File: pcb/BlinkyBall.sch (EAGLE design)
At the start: 18 parts, among them U1 Tiny85-20-SMT

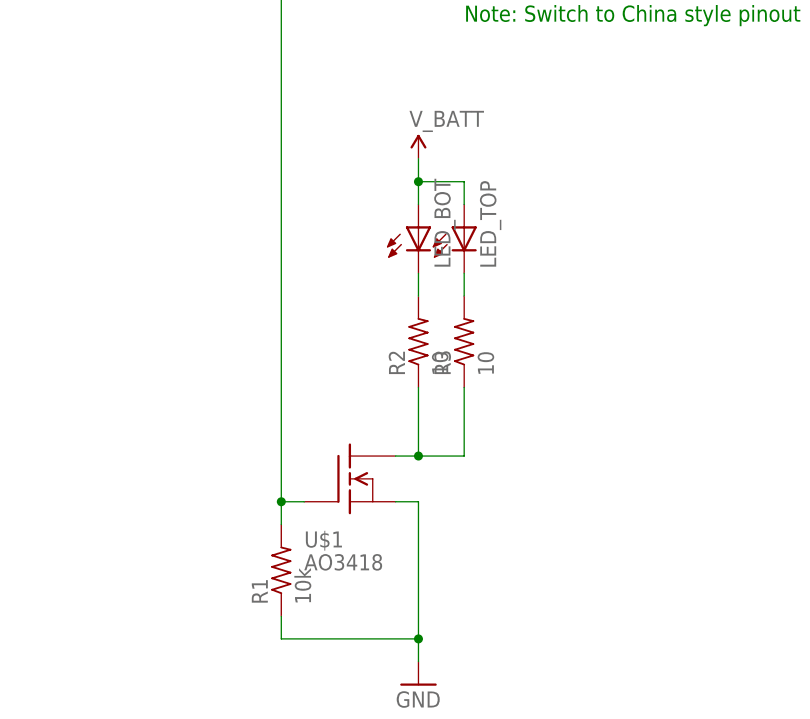
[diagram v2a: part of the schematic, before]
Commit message: PCB: Fix referene names
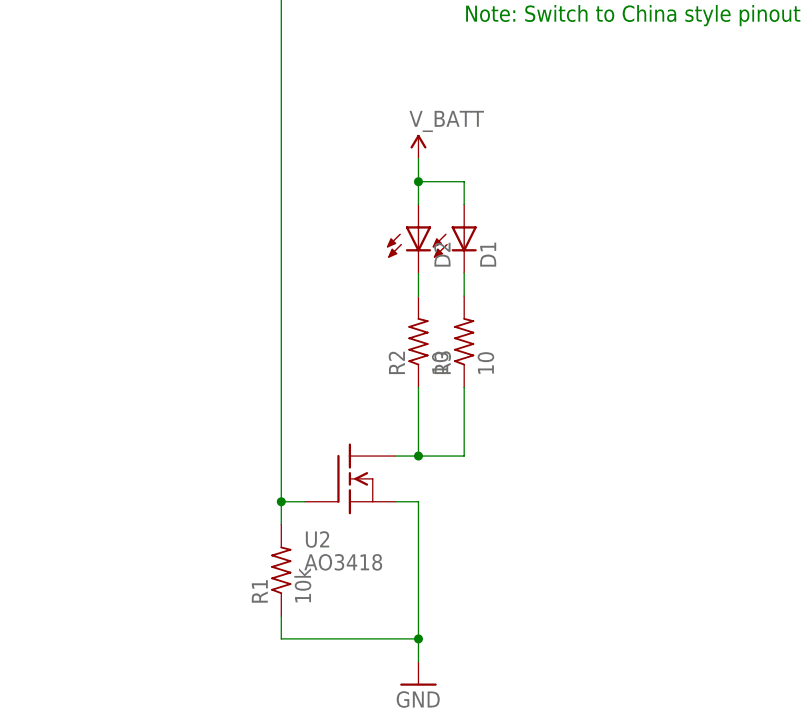
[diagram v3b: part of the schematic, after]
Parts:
- renumbered LED_BOT to D2, LED_TOP to D1, U$1 to U2, U$2 to J2, U$3 to J1, U$5 to U3
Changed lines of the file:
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@@
 <parts>
 <part name="U1" library="SparkFun-DigitalIC" deviceset="ATTINY45" device="TINY85-20-SMT" value="Tiny85-20-SMT"/>
-<part name="U$2" library="blinkinlabs" deviceset="BATTERY_BUTTON_CELL" device="AG3" value="BATTERY_BUTTON_CELLAG3"/>
+<part name="J2" library="blinkinlabs" deviceset="BATTERY_BUTTON_CELL" device="AG3" value="BATTERY_BUTTON_CELLAG3"/>
 <part name="SUPPLY1" library="SparkFun-Aesthetics" deviceset="V_BATT" device=""/>
 <part name="GND1" library="SparkFun-Aesthetics" deviceset="GND" device=""/>
@@
 <part name="GND2" library="SparkFun-Aesthetics" deviceset="GND" device=""/>
 <part name="C1" library="adafruit" deviceset="C-US" device="C0603" value="100nF"/>
-<part name="U$5" library="blinkinlabs" deviceset="TSOP321" device=""/>
+<part name="U3" library="blinkinlabs" deviceset="TSOP321" device=""/>
 <part name="R2" library="adafruit" deviceset="R-US_" device="R0603" value="10"/>
 <part name="R3" library="adafruit" deviceset="R-US_" device="R0603" value="10"/>
@@
 <part name="TP5" library="SparkFun-Passives" deviceset="TEST-POINT" device="3X5"/>
 <part name="TP6" library="SparkFun-Passives" deviceset="TEST-POINT" device="3X5"/>
-<part name="LED_BOT" library="adafruit" deviceset="LED" device="5MM"/>
-<part name="LED_TOP" library="adafruit" deviceset="LED" device="5MM"/>
+<part name="D2" library="adafruit" deviceset="LED" device="5MM"/>
+<part name="D1" library="adafruit" deviceset="LED" device="5MM"/>
 <part name="GND5" library="SparkFun-Aesthetics" deviceset="GND" device=""/>
-<part name="U$1" library="blinkinlabs" deviceset="N_MOSFET" device="SOT23" value="AO3418"/>
+<part name="U2" library="blinkinlabs" deviceset="N_MOSFET" device="SOT23" value="AO3418"/>
 <part name="SUPPLY5" library="SparkFun-Aesthetics" deviceset="V_BATT" device=""/>
 <part name="R1" library="adafruit" deviceset="R-US_" device="R0603" value="10k"/>
 <part name="GND4" library="SparkFun-Aesthetics" deviceset="GND" device=""/>
-<part name="U$3" library="blinkinlabs" deviceset="SW-18015P" device=""/>
+<part name="J1" library="blinkinlabs" deviceset="SW-18015P" device=""/>
 </parts>
 <sheets>
@@
 <instances>
 <instance part="U1" gate="G$1" x="30.48" y="68.58"/>
-<instance part="U$2" gate="G$1" x="-33.02" y="68.58"/>
+<instance part="J2" gate="G$1" x="-33.02" y="68.58"/>
 <instance part="SUPPLY1" gate="G$1" x="-33.02" y="83.82"/>
 <instance part="GND1" gate="1" x="-33.02" y="53.34"/>
@@
 <instance part="GND2" gate="1" x="7.62" y="50.8"/>
 <instance part="C1" gate="G$1" x="12.7" y="71.12"/>
-<instance part="U$5" gate="G$1" x="116.84" y="68.58"/>
+<instance part="U3" gate="G$1" x="116.84" y="68.58"/>
 <instance part="R2" gate="G$1" x="93.98" y="25.4" rot="R90"/>
 <instance part="R3" gate="G$1" x="99.06" y="25.4" rot="R90"/>
@@
 <instance part="TP5" gate="G$1" x="2.54" y="63.5" rot="R180"/>
 <instance part="TP6" gate="G$1" x="45.72" y="83.82" rot="R90"/>
-<instance part="LED_BOT" gate="G$1" x="93.98" y="38.1"/>
-<instance part="LED_TOP" gate="G$1" x="99.06" y="38.1"/>
+<instance part="D2" gate="G$1" x="93.98" y="38.1"/>
+<instance part="D1" gate="G$1" x="99.06" y="38.1"/>
 <instance part="GND5" gate="1" x="93.98" y="-12.7"/>
-<instance part="U$1" gate="G$1" x="83.82" y="10.16"/>
+<instance part="U2" gate="G$1" x="83.82" y="10.16"/>
 <instance part="SUPPLY5" gate="G$1" x="93.98" y="45.72"/>
 <instance part="R1" gate="G$1" x="78.74" y="0" rot="R90"/>
 <instance part="GND4" gate="1" x="99.06" y="73.66"/>
-<instance part="U$3" gate="G$1" x="99.06" y="91.44" rot="MR0"/>
+<instance part="J1" gate="G$1" x="99.06" y="91.44" rot="MR0"/>
 </instances>
 <busses>
@@
 <segment>
 <pinref part="SUPPLY1" gate="G$1" pin="V_BATT"/>
-<pinref part="U$2" gate="G$1" pin="+"/>
+<pinref part="J2" gate="G$1" pin="+"/>
 <wire x1="-33.02" y1="83.82" x2="-33.02" y2="78.74" width="0.1524" layer="91"/>
 </segment>
@@
 </segment>
 <segment>
-<pinref part="LED_TOP" gate="G$1" pin="A"/>
+<pinref part="D1" gate="G$1" pin="A"/>
 <wire x1="99.06" y1="40.64" x2="99.06" y2="43.18" width="0.1524" layer="91"/>
 <wire x1="99.06" y1="43.18" x2="93.98" y2="43.18" width="0.1524" layer="91"/>
 <pinref part="SUPPLY5" gate="G$1" pin="V_BATT"/>
 <wire x1="93.98" y1="43.18" x2="93.98" y2="45.72" width="0.1524" layer="91"/>
-<pinref part="LED_BOT" gate="G$1" pin="A"/>
+<pinref part="D2" gate="G$1" pin="A"/>
 <wire x1="93.98" y1="43.18" x2="93.98" y2="40.64" width="0.1524" layer="91"/>
 <junction x="93.98" y="43.18"/>
@@
 <net name="GND" class="0">
 <segment>
-<pinref part="U$2" gate="G$1" pin="-"/>
+<pinref part="J2" gate="G$1" pin="-"/>
 <wire x1="-33.02" y1="60.96" x2="-33.02" y2="55.88" width="0.1524" layer="91"/>
 <pinref part="GND1" gate="1" pin="GND"/>
@@
 <pinref part="GND5" gate="1" pin="GND"/>
 <wire x1="93.98" y1="7.62" x2="93.98" y2="-7.62" width="0.1524" layer="91"/>
-<pinref part="U$1" gate="G$1" pin="S"/>
+<pinref part="U2" gate="G$1" pin="S"/>
 <pinref part="R1" gate="G$1" pin="1"/>
 <wire x1="93.98" y1="-7.62" x2="93.98" y2="-10.16" width="0.1524" layer="91"/>
@@
 <pinref part="GND3" gate="1" pin="GND"/>
 <wire x1="116.84" y1="91.44" x2="116.84" y2="88.9" width="0.1524" layer="91"/>
-<pinref part="U$3" gate="G$1" pin="P$1"/>
+<pinref part="J1" gate="G$1" pin="P$1"/>
 <wire x1="111.76" y1="91.44" x2="116.84" y2="91.44" width="0.1524" layer="91"/>
 </segment>
 <segment>
-<pinref part="U$5" gate="G$1" pin="VS"/>
+<pinref part="U3" gate="G$1" pin="VS"/>
 <pinref part="GND4" gate="1" pin="GND"/>
 <wire x1="111.76" y1="71.12" x2="109.22" y2="71.12" width="0.1524" layer="91"/>
@@
 <wire x1="53.34" y1="83.82" x2="53.34" y2="71.12" width="0.1524" layer="91"/>
 <junction x="53.34" y="71.12"/>
-<pinref part="U$3" gate="G$1" pin="P$2"/>
+<pinref part="J1" gate="G$1" pin="P$2"/>
 <wire x1="96.52" y1="91.44" x2="93.98" y2="91.44" width="0.1524" layer="91"/>
 <junction x="93.98" y="91.44"/>
@@
 <wire x1="78.74" y1="73.66" x2="78.74" y2="7.62" width="0.1524" layer="91"/>
 <wire x1="81.28" y1="7.62" x2="78.74" y2="7.62" width="0.1524" layer="91"/>
-<pinref part="U$1" gate="G$1" pin="G"/>
+<pinref part="U2" gate="G$1" pin="G"/>
 <pinref part="R1" gate="G$1" pin="2"/>
 <wire x1="78.74" y1="7.62" x2="78.74" y2="5.08" width="0.1524" layer="91"/>
@@
 <wire x1="111.76" y1="66.04" x2="43.18" y2="66.04" width="0.1524" layer="91"/>
 <pinref part="U1" gate="G$1" pin="PB4(ADC2)"/>
-<pinref part="U$5" gate="G$1" pin="GND"/>
+<pinref part="U3" gate="G$1" pin="GND"/>
 </segment>
 </net>
@@
 <pinref part="U1" gate="G$1" pin="PB3(ADC3)"/>
 <wire x1="43.18" y1="68.58" x2="111.76" y2="68.58" width="0.1524" layer="91"/>
-<pinref part="U$5" gate="G$1" pin="OUT"/>
+<pinref part="U3" gate="G$1" pin="OUT"/>
 </segment>
 </net>
@@
 <net name="N$2" class="0">
 <segment>
-<pinref part="LED_BOT" gate="G$1" pin="C"/>
+<pinref part="D2" gate="G$1" pin="C"/>
 <pinref part="R2" gate="G$1" pin="2"/>
 <wire x1="93.98" y1="33.02" x2="93.98" y2="30.48" width="0.1524" layer="91"/>
@@
 <net name="N$3" class="0">
 <segment>
-<pinref part="LED_TOP" gate="G$1" pin="C"/>
+<pinref part="D1" gate="G$1" pin="C"/>
 <pinref part="R3" gate="G$1" pin="2"/>
 <wire x1="99.06" y1="33.02" x2="99.06" y2="30.48" width="0.1524" layer="91"/>
@@
 <pinref part="R2" gate="G$1" pin="1"/>
 <wire x1="93.98" y1="20.32" x2="93.98" y2="12.7" width="0.1524" layer="91"/>
-<pinref part="U$1" gate="G$1" pin="D"/>
+<pinref part="U2" gate="G$1" pin="D"/>
 <wire x1="93.98" y1="12.7" x2="91.44" y2="12.7" width="0.1524" layer="91"/>
 <pinref part="R3" gate="G$1" pin="1"/>

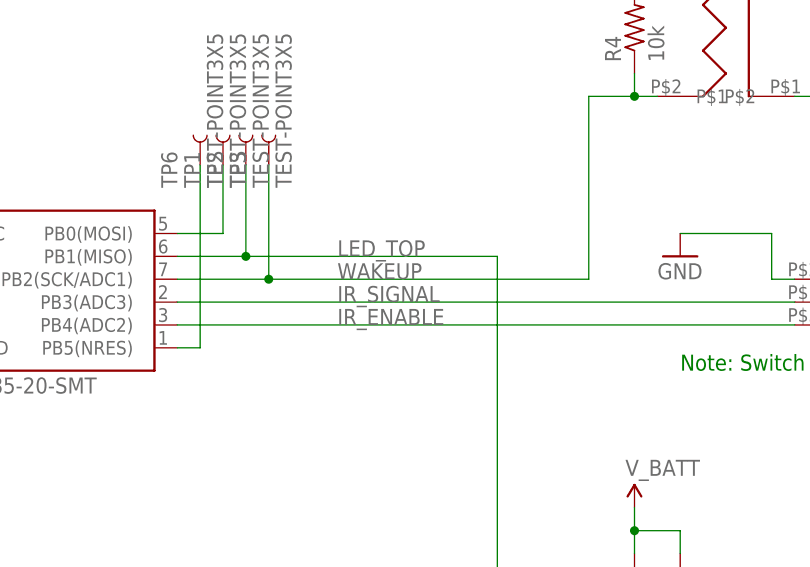
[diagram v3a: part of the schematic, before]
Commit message: Correct pinout for IR receiver
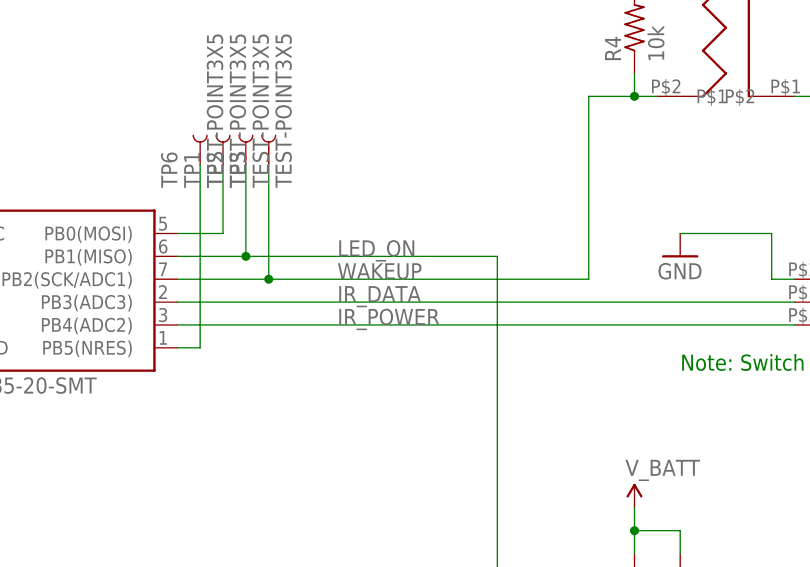
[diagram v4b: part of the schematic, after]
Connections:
- net IR_ENABLE renamed IR_POWER
- net IR_SIGNAL renamed IR_DATA
- net LED_TOP renamed LED_ON
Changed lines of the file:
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@@
 </segment>
 </net>
-<net name="LED_TOP" class="0">
+<net name="LED_ON" class="0">
 <segment>
 <pinref part="U1" gate="G$1" pin="PB1(MISO)"/>
@@
 </segment>
 </net>
-<net name="IR_ENABLE" class="0">
+<net name="IR_POWER" class="0">
 <segment>
 <label x="60.96" y="66.04" size="1.778" layer="95"/>
@@
 </segment>
 </net>
-<net name="IR_SIGNAL" class="0">
+<net name="IR_DATA" class="0">
 <segment>
 <label x="60.96" y="68.58" size="1.778" layer="95"/>

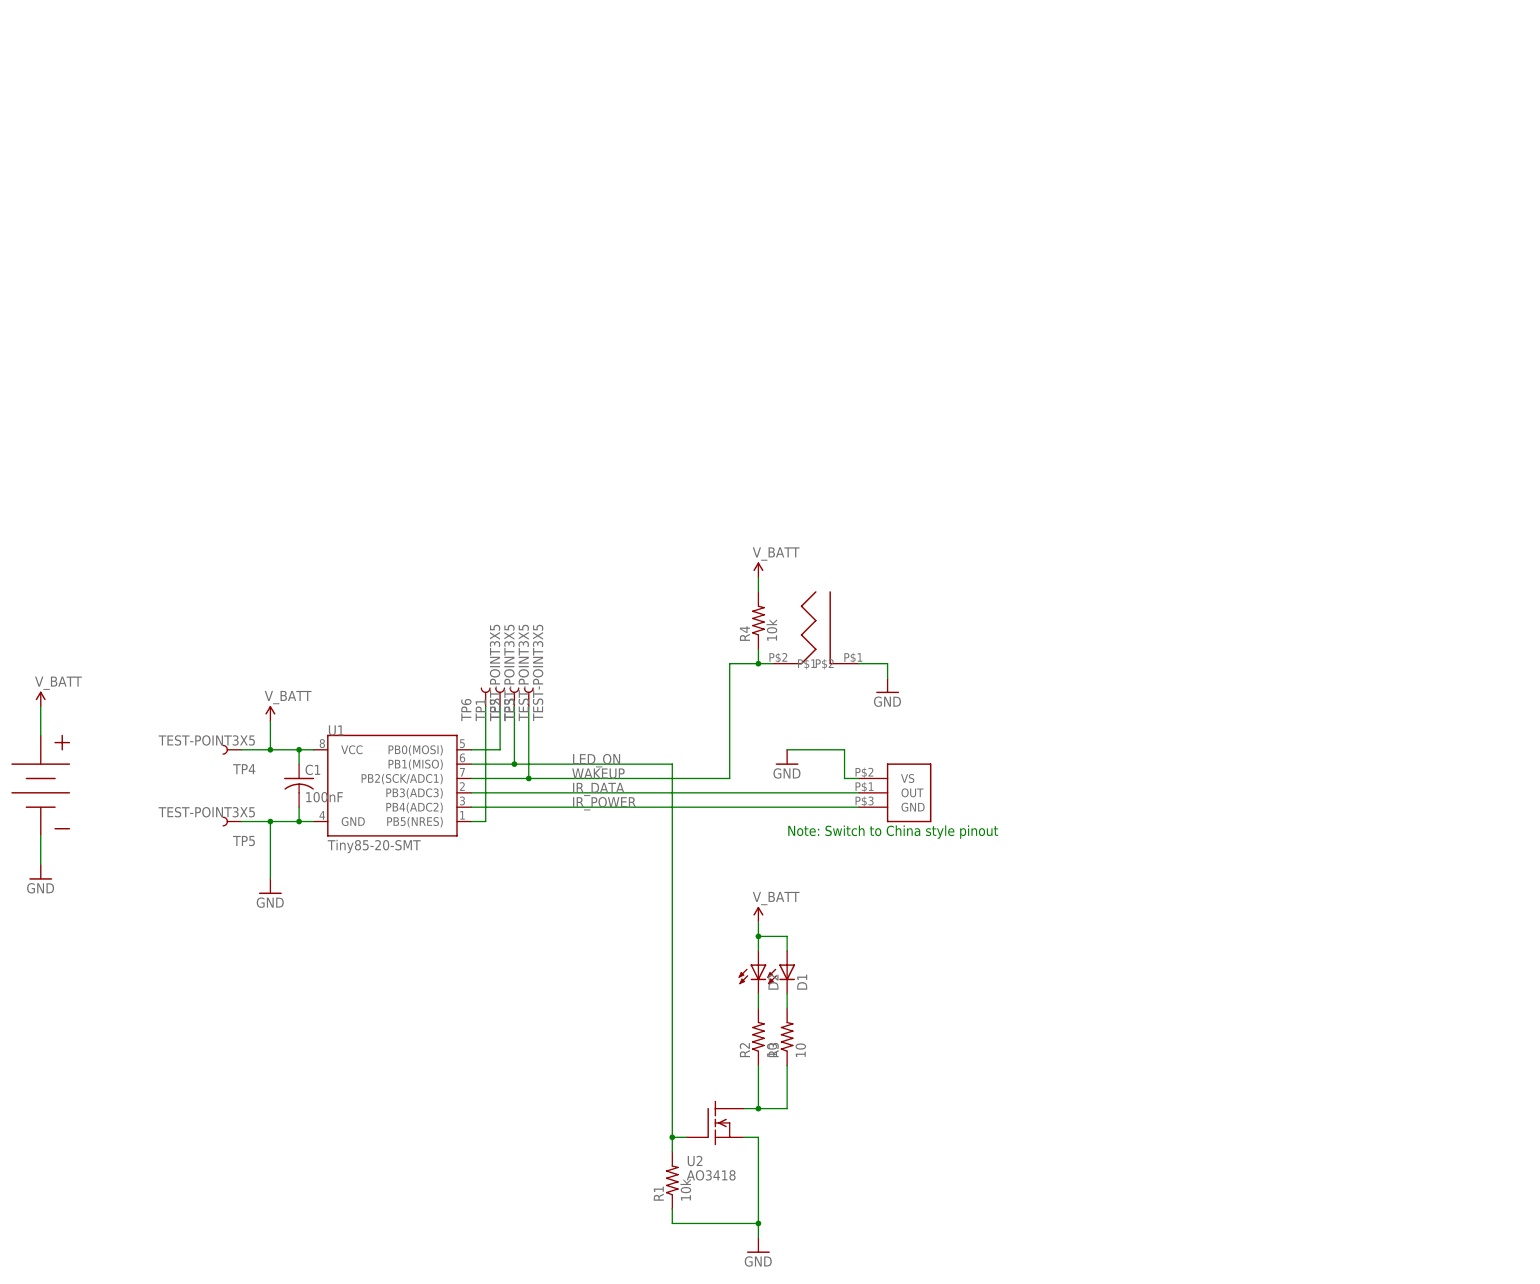
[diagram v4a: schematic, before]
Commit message: Remove old schematic design, add release files for production version
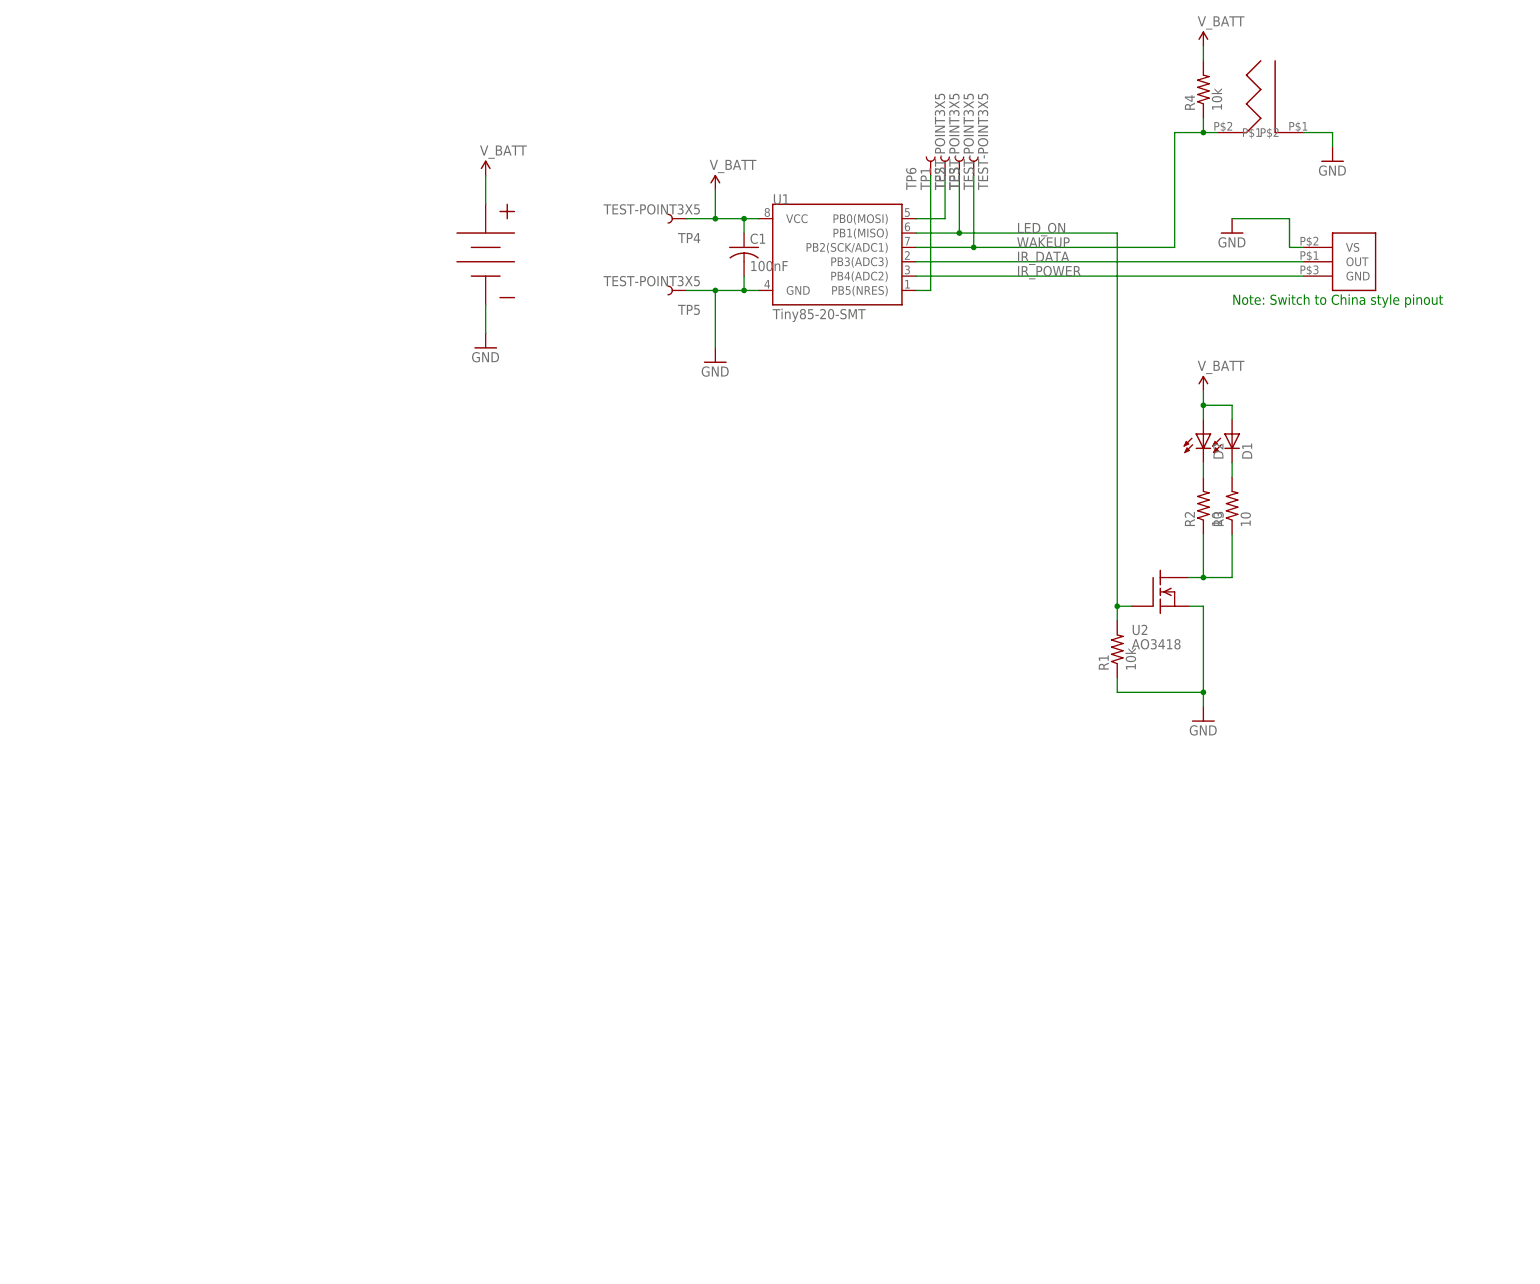
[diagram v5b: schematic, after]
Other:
- moved on the sheet: C1, D1, D2, R1, R2, R3, R4, TP1, TP2, TP3, TP4, TP5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
